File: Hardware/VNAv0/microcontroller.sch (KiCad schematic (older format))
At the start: 64 parts, among them SW1 SW_Push, SW2 SW_Push, SW3 SW_Push, U16 STM32F373RCTx, U17 AT25SF081-SSHD-X, Y1 8MHz

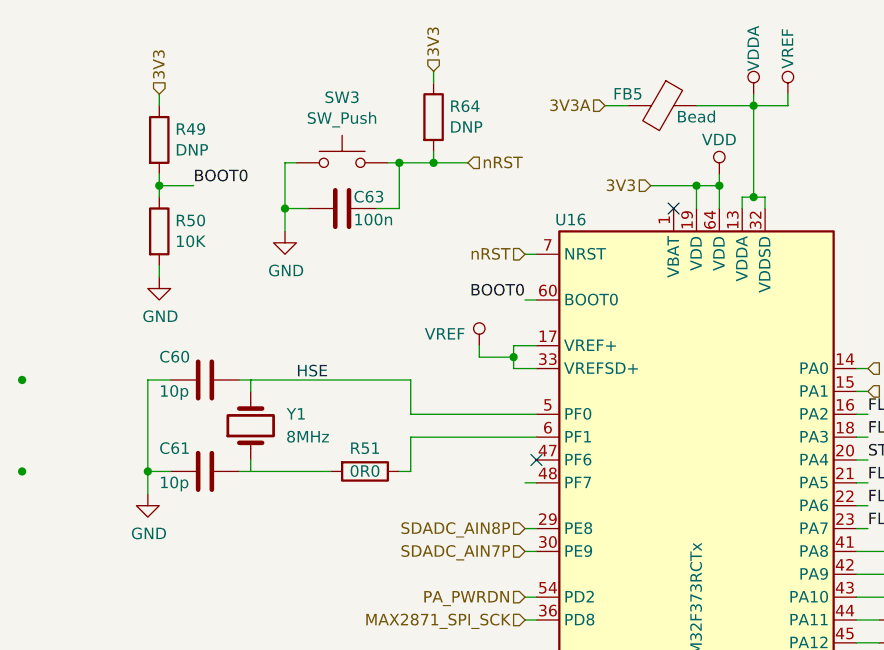
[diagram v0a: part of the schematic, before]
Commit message: tx chain now works, however output power too low
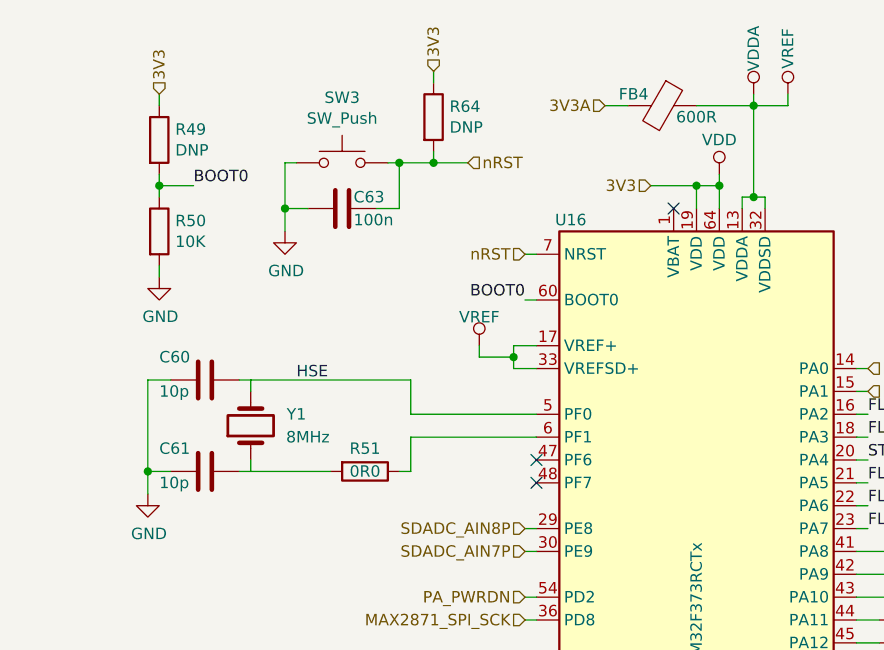
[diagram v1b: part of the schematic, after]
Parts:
- removed FB5: Bead, VNA_Footprints:BEADC1608X95N, symbol VNA_Symbols:Ferrite_Bead_PWR
- added FB4: 600R, symbol VNA_Symbols:Ferrite_Bead_PWR
- D15: footprint VNA_Footprints:ARGB_PLCC4_1210_LED -> (none)
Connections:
- net 3V3A: now also FB4.2
- net VDDA: now also FB4.1
- no-connect marks 4 -> 5
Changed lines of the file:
@@
 	1450 7100 1800 7100
-$Comp
-L VNA_Symbols:VREF #PWR0110
-U 1 1 5CC151AE
-P 2250 7050
-F 0 "#PWR0110" H 2250 6900 50  0001 C CNN
-F 1 "VREF" H 2267 7223 50  0000 C CNN
-F 2 "" H 2250 7050 50  0001 C CNN
-F 3 "" H 2250 7050 50  0001 C CNN
-	1    2250 7050
-	1    0    0    -1
-$EndComp
 $Comp
 L Device:C C72
@@
 Wire Wire Line
 	3400 1100 3400 1150
-$Comp
-L VNA_Symbols:VREF #PWR0109
-U 1 1 5CC361B6
-P 3400 1100
-F 0 "#PWR0109" H 3400 950 50  0001 C CNN
-F 1 "VREF" V 3400 1300 50  0000 C CNN
-F 2 "" H 3400 1100 50  0001 C CNN
-F 3 "" H 3400 1100 50  0001 C CNN
-	1    3400 1100
-	1    0    0    -1
-$EndComp
 Wire Wire Line
 	2050 2250 2200 2250
 Wire Wire Line
 	2050 2200 2050 2250
-$Comp
-L VNA_Symbols:VREF #PWR0103
-U 1 1 5CC32AC4
-P 2050 2200
-F 0 "#PWR0103" H 2050 2050 50  0001 C CNN
-F 1 "VREF" H 1900 2250 50  0000 C CNN
-F 2 "" H 2050 2200 50  0001 C CNN
-F 3 "" H 2050 2200 50  0001 C CNN
-	1    2050 2200
-	1    0    0    -1
-$EndComp
 Wire Wire Line
 	2200 2250 2200 2200
@@
 Wire Wire Line
 	1700 2750 1750 2750
-Connection ~ 50   2750
 Wire Wire Line
 	1400 2750 1050 2750
@@
 Text Notes 1250 2350 0    50   ~ 0
 HSE
-Connection ~ 50   2350
 Wire Wire Line
 	1750 2350 1050 2350
@@
 Text HLabel 3750 3800 2    50   Input ~ 0
 SCL
-$Comp
-L VNA_Symbols:Ferrite_Bead_PWR FB?
-U 1 1 5CC6BC19
-P 2850 1150
-AR Path="/5CC6BC19" Ref="FB?"  Part="1"
-AR Path="/5CAA2138/5CC6BC19" Ref="FB5"  Part="1"
-F 0 "FB5" V 2800 1000 50  0000 C CNN
-F 1 "Bead" V 2900 1300 50  0000 C CNN
-F 2 "VNA_Footprints:BEADC1608X95N" V 2780 1150 50  0001 C CNN
-F 3 "~" H 2850 1150 50  0001 C CNN
-	1    2850 1150
-	0    1    1    0
-$EndComp
 NoConn ~ 2300 2700
 $Comp
@@
 	1    2250 7300
 	1    0    0    -1
-$EndComp
-$Comp
-L VNA_Symbols:LED_RGBA D15
-U 1 1 5CBE1B64
-P 6050 4600
-F 0 "D15" H 6050 5097 50  0000 C CNN
-F 1 "LED_RGBA" H 6050 5006 50  0000 C CNN
-F 2 "VNA_Footprints:ARGB_PLCC4_1210_LED" H 6050 4550 50  0001 C CNN
-F 3 "~" H 6050 4550 50  0001 C CNN
-	1    6050 4600
-	-1   0    0    -1
 $EndComp
 $Comp
@@
 ATTEN_MISO
 Wire Wire Line
-	2250 2800 2300 2800
-Wire Wire Line
 	1750 2600 2300 2600
 Wire Wire Line
@@
 	0    1    1    0
 $EndComp
+$Comp
+L VNA_Symbols:LED_RGBA D15
+U 1 1 5D18DC39
+P 6050 4600
+F 0 "D15" H 6050 5097 50  0000 C CNN
+F 1 "LED_RGBA" H 6050 5006 50  0000 C CNN
+F 2 "" H 6050 4550 50  0001 C CNN
+F 3 "~" H 6050 4550 50  0001 C CNN
+	1    6050 4600
+	-1   0    0    -1
+$EndComp
+$Comp
+L VNA_Symbols:VREF #PWR0103
+U 1 1 5D18F083
+P 2250 7050
+F 0 "#PWR0103" H 2250 6900 50  0001 C CNN
+F 1 "VREF" H 2267 7223 50  0000 C CNN
+F 2 "" H 2250 7050 50  0001 C CNN
+F 3 "" H 2250 7050 50  0001 C CNN
+	1    2250 7050
+	1    0    0    -1
+$EndComp
+$Comp
+L VNA_Symbols:VREF #PWR0109
+U 1 1 5D1902B3
+P 2050 2200
+F 0 "#PWR0109" H 2050 2050 50  0001 C CNN
+F 1 "VREF" H 2050 2325 50  0000 C CNN
+F 2 "" H 2050 2200 50  0001 C CNN
+F 3 "" H 2050 2200 50  0001 C CNN
+	1    2050 2200
+	1    0    0    -1
+$EndComp
+$Comp
+L VNA_Symbols:VREF #PWR0110
+U 1 1 5D190BD1
+P 3400 1100
+F 0 "#PWR0110" H 3400 950 50  0001 C CNN
+F 1 "VREF" V 3400 1300 50  0000 C CNN
+F 2 "" H 3400 1100 50  0001 C CNN
+F 3 "" H 3400 1100 50  0001 C CNN
+	1    3400 1100
+	1    0    0    -1
+$EndComp
+$Comp
+L VNA_Symbols:Ferrite_Bead_PWR FB4
+U 1 1 5D1914BF
+P 2850 1150
+F 0 "FB4" V 2800 1025 50  0000 C CNN
+F 1 "600R" V 2900 1300 50  0000 C CNN
+F 2 "" V 2780 1150 50  0001 C CNN
+F 3 "~" H 2850 1150 50  0001 C CNN
+	1    2850 1150
+	0    1    1    0
+$EndComp
+NoConn ~ 2300 2800
 $EndSCHEMATC
